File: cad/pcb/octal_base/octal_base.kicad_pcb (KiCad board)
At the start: 2 copper layers, 24.8 x 24.8 mm, 9 parts, among them J1 U6A Base, J2 Pin header

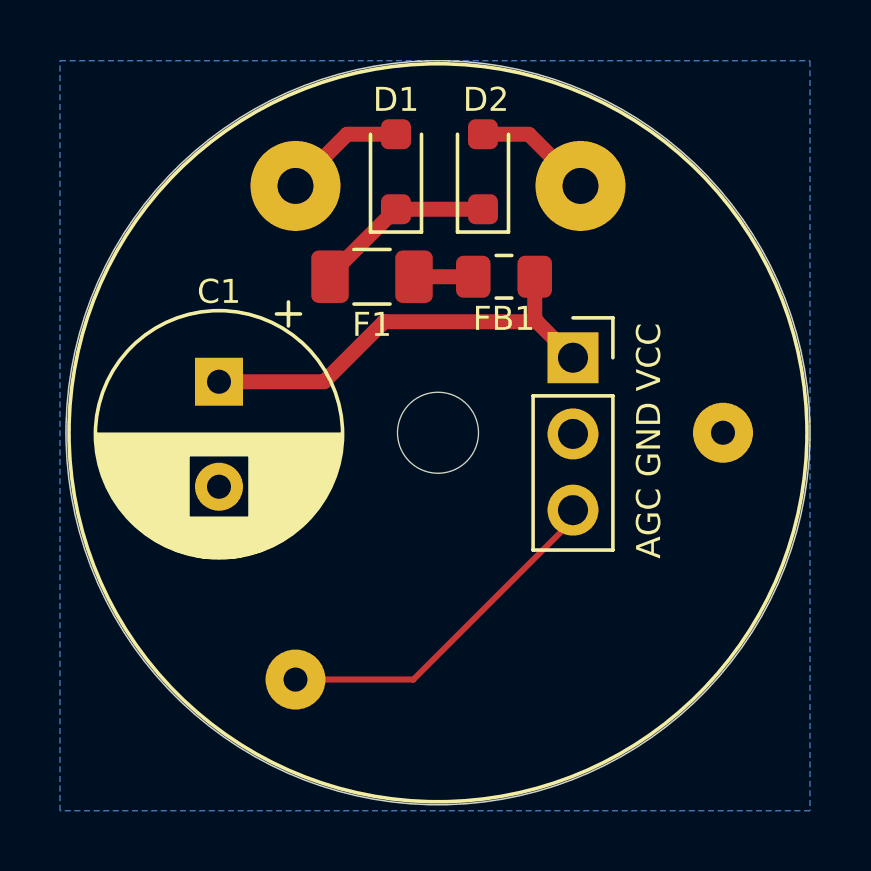
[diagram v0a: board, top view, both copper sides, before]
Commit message: Change: Pcb to octal
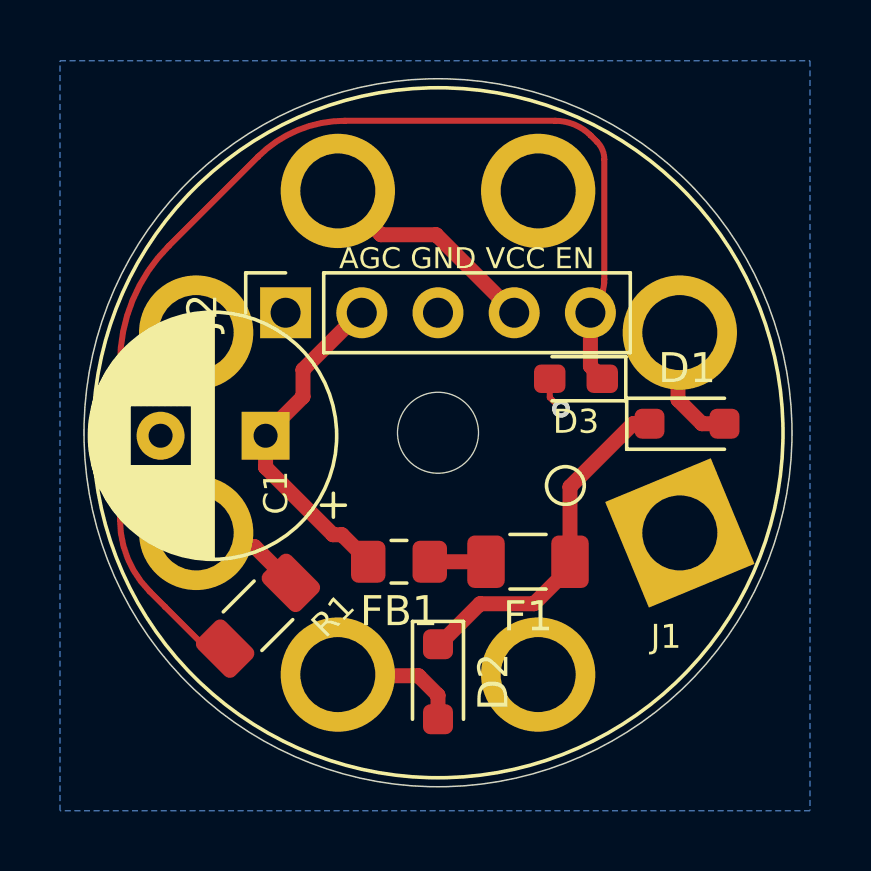
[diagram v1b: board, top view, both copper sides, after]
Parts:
- removed G***: LOGO, Icons_Graphics:retronics_logo_14mm
- added D3: 3.3V, Diode_SMD:D_0603_1608Metric_Pad1.05x0.95mm_HandSolder, F.Cu at (95.2, 75.1)
- added R1: 1M, Resistor_SMD:R_1206_3216Metric_Pad1.30x1.75mm_HandSolder, F.Cu at (84.6, 83.0)
- D1, D2: value 1N5819WS -> 1N5819W; footprint Retronics_Discrete:D_SOD-323_HandSoldering -> Diode_SMD:D_SOD-323_HandSoldering
- F1: footprint Retronics_Passives:Fuse_1206_3216Metric -> Fuse:Fuse_1206_3216Metric
- FB1: footprint Retronics_Passives:L_0805_2012Metric_Pad1.15x1.40mm_HandSolder -> Inductor_SMD:L_0805_2012Metric_Pad1.15x1.40mm_HandSolder
- J1: value U6A Base -> Octal Base; footprint Retronics_Connectors:U6A_Base -> Library:Valve_Octal_Base
- J2: value Pin header -> Pin Socket; footprint Retronics_Connectors:PinSocket_1x03_P2.54mm_Vertical -> Connector_PinSocket_2.54mm:PinSocket_1x05_P2.54mm_Vertical
- moved D2 17.1 mm to (90.6, 85.2), turned to -90 degrees
- moved D1 12.8 mm to (98.9, 76.6), turned to 0 degrees
- moved F1 10.8 mm to (93.6, 81.2), turned to 180 degrees
- moved FB1 10.1 mm to (89.3, 81.2), turned to 180 degrees
- moved J2 9.70 mm to (85.5, 72.9), turned to 90 degrees
- moved J1 8.73 mm to (98.7, 80.2), turned to 22.5 degrees
- moved C1 2.38 mm to (84.9, 77.0), turned to 180 degrees
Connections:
- J1 pad 1: H1 -> unconnected-(J1-Pin_1-Pad1)
- J1 pad 3: AGC -> unconnected-(J1-Pin_3-Pad3)
- J1 pad 5: GND -> unconnected-(J1-Pin_5-Pad5)
- J1 pad 6: H2 -> Net-(J1-Pin_6)
- J2 pad 1: VCC -> unconnected-(J2-Pin_1-Pad1)
- J2 pad 2: GND -> VCC
- J2 pad 3: AGC -> GND
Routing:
- net EN: track 0.00 -> 39.5 mm
- net Net-(D1-K): track 6.06 -> 11.7 mm
- net AGC: track 11.9 -> 7.50 mm
- net VCC: track 14.7 -> 11.2 mm
- net Net-(J1-Pin_6): track 0.00 -> 2.29 mm
- net GND: track 0.00 -> 1.16 mm, vias 0 -> 1
- net H2: track 3.96 -> 3.17 mm
- net H1: track 4.06 -> 3.38 mm
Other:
- board size 24.8 x 24.8 mm -> 23.6 x 23.6 mm
- board text added: "AGC GND VCC EN"
- board text added: "EM34 Tube Base DL2WAG Martin Wagner"
- board text removed: "AGC GND VCC"
- board text removed: "U6A Tube Base R0179_2429 Bjørner Sandom"

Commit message: Fix: EM34 commonly uses cathode resistor, can't use k as gnd
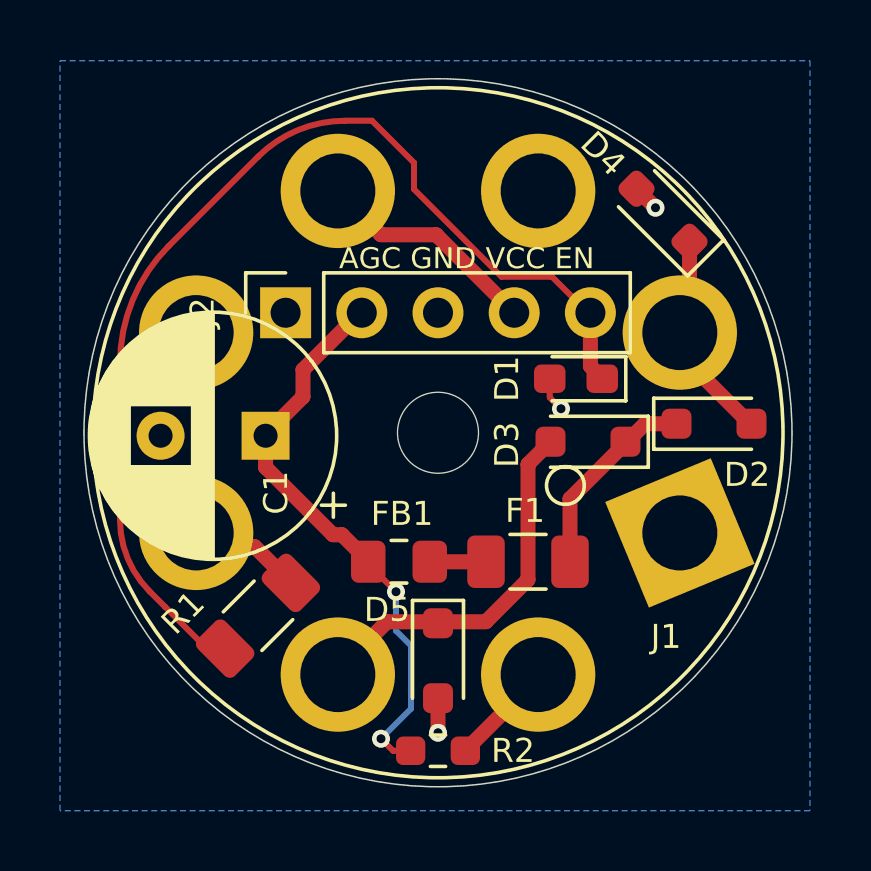
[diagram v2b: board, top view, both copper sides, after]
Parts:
- added D4: 1N5819W, Diode_SMD:D_SOD-323_HandSoldering, F.Cu at (98.1, 69.7)
- added D5: 1N5819W, Diode_SMD:D_SOD-323_HandSoldering, F.Cu at (90.6, 84.5)
- added R2: 4k7, Resistor_SMD:R_0603_1608Metric_Pad0.98x0.95mm_HandSolder, F.Cu at (90.6, 87.5)
- D1: value 1N5819W -> 3.3V; footprint Diode_SMD:D_SOD-323_HandSoldering -> Diode_SMD:D_0603_1608Metric_Pad1.05x0.95mm_HandSolder
- D3: value 3.3V -> 1N5819W; footprint Diode_SMD:D_0603_1608Metric_Pad1.05x0.95mm_HandSolder -> Diode_SMD:D_SOD-323_HandSoldering
- moved D2 12.6 mm to (99.8, 76.6), turned to 0 degrees
- moved D1 3.99 mm to (95.2, 75.1), turned to 180 degrees
- moved D3 2.14 mm to (95.6, 77.2)
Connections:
- D1 pad 1: Net-(D1-K) -> EN
- D1 pad 2: H1 -> GND
- D2 pad 1: Net-(D1-K) -> Net-(D2-K)
- D2 pad 2: H2 -> H1
- D3 pad 1: EN -> Net-(D2-K)
- D3 pad 2: GND -> H2
- F1 pad 1: Net-(D1-K) -> Net-(D2-K)
- J1 pad 8: GND -> K
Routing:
- net Net-(D1-K): track 11.7 -> 0.00 mm
- net H2: track 3.17 -> 12.4 mm
- net VCC: track 11.2 -> 19.3 mm, vias 0 -> 2
- net Net-(D2-K): track 0.00 -> 6.79 mm
- net K: track 0.00 -> 3.11 mm
- net EN: track 39.5 -> 36.9 mm
- net H1: track 3.38 -> 5.84 mm
- net GND: track 1.16 -> 3.20 mm, vias 1 -> 3

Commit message: Add: Base Cleanup
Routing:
- net GND: track 3.20 -> 6.02 mm, vias 3 -> 5

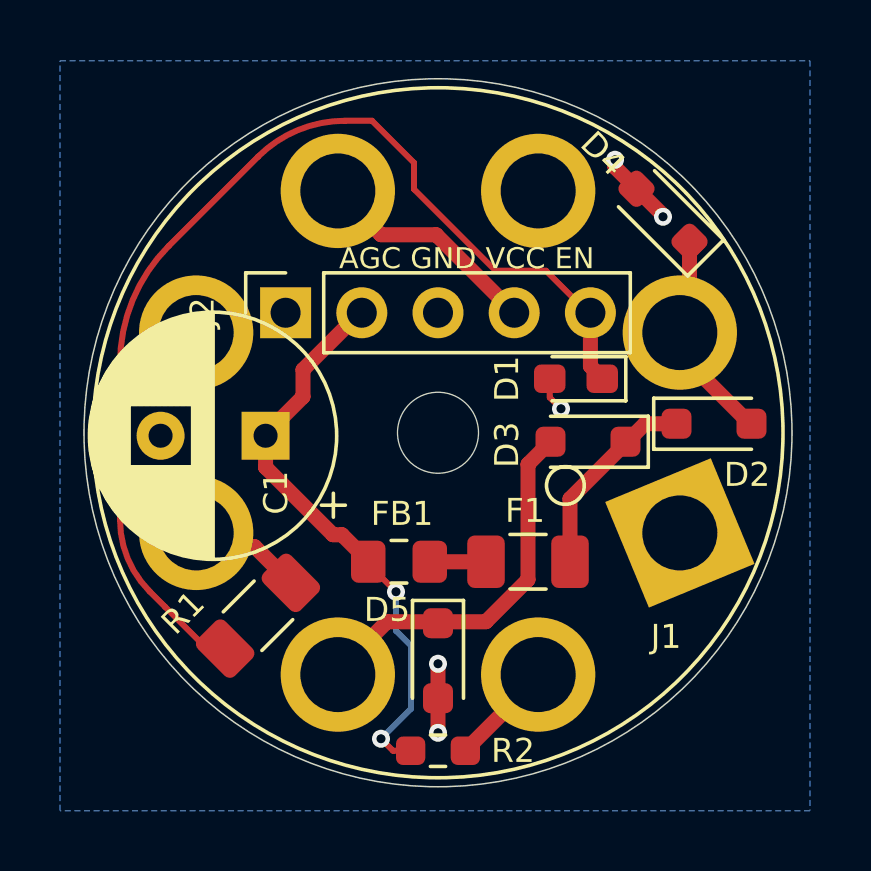
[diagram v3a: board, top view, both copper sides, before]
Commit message: Fix: EM34 socket, don't use bridge rect...
gnd floats at approx. 1/2 vcc relative to chassis-gnd -- oops.
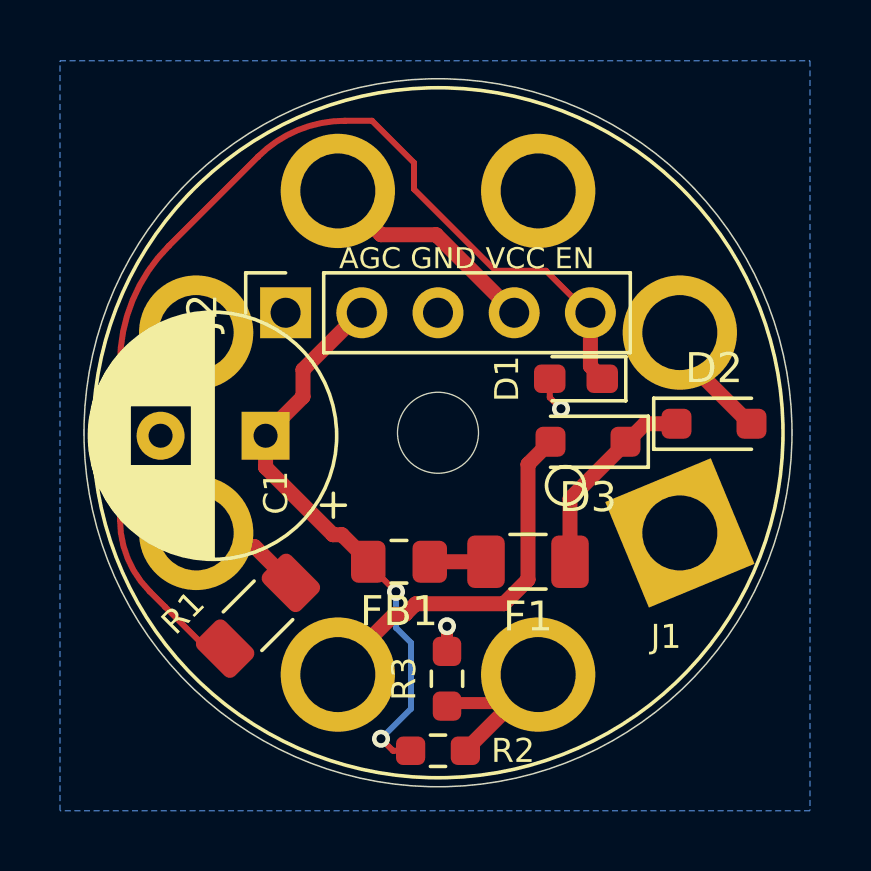
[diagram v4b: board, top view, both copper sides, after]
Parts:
- removed D4, D5: 1N5819W, Diode_SMD:D_SOD-323_HandSoldering
- added R3: 0, Resistor_SMD:R_0603_1608Metric_Pad0.98x0.95mm_HandSolder, F.Cu at (90.9, 85.1)
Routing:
- net GND: track 6.02 -> 1.79 mm, vias 5 -> 2
- net H1: track 5.84 -> 4.11 mm
- net K: track 3.11 -> 4.69 mm
